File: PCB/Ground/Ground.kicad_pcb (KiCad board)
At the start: 2 copper layers, 100 x 86.6 mm, 39 parts, among them CN1 GROVE, CN2 GROVE, CN3 GROVE, CN4 GROVE, CN5 GROVE, CN6 TTL-232R-3V3, CN7 ST-LINK, CN8 Conn_01x05_Female, CN9 CardEdgeConnector5P, SW1 RESET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

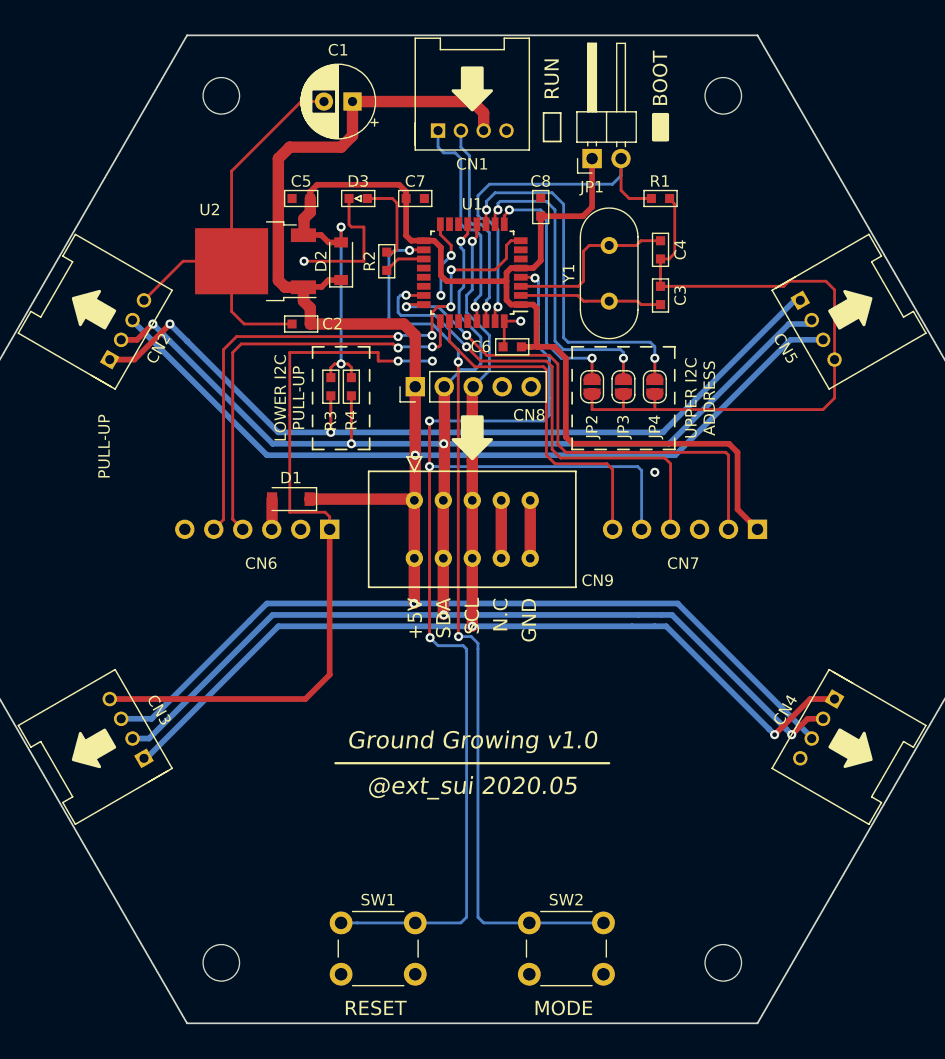
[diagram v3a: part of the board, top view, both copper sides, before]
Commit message: [update] Groundの配線改善(GNDビア) #4
* GNDビアを10mm間隔で配置できる箇所に配置
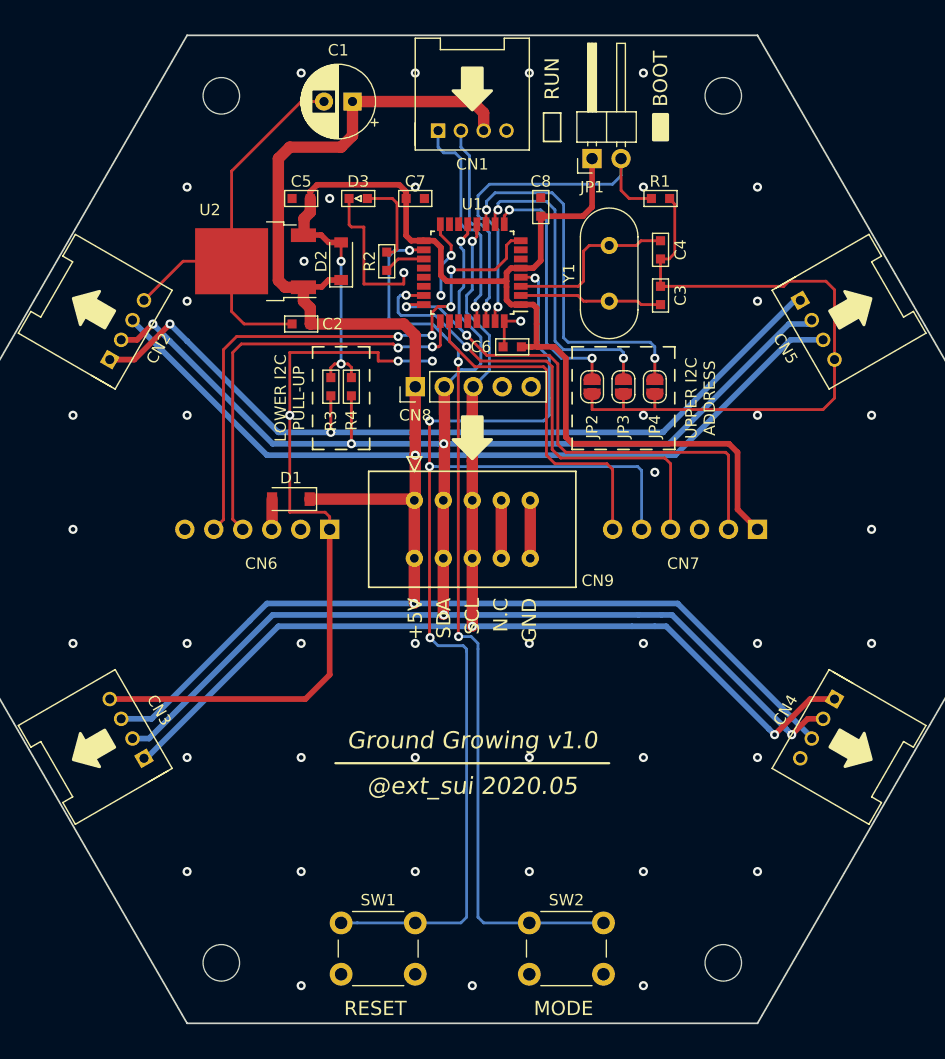
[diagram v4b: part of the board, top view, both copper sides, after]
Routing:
- net 3V3: track 109.0 -> 106.3 mm
- net GND: track 191.7 -> 192.9 mm, vias 7 -> 50
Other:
- board text removed: "PULL-UP"
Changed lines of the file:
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@@
   (general
     (thickness 1.6)
-    (drawings 114)
-    (tracks 506)
+    (drawings 113)
+    (tracks 550)
     (zones 0)
     (modules 39)
@@
   )
   (setup
-    (last_trace_width 0.5)
+    (last_trace_width 0.25)
     (user_trace_width 0.5)
     (user_trace_width 1)
@@
     (descr "Through hole straight pin header, 1x05, 2.54mm pitch, single row")
     (tags "Through hole pin header THT 1x05 2.54mm single row")
-    (fp_text reference CN8 (at -2.5 10 180) (layer F.SilkS)
+    (fp_text reference CN8 (at -2.5 0 180) (layer F.SilkS)
       (effects (font (size 1 1) (thickness 0.15)))
     )
@@
   (gr_line (start 120 89) (end 121 89) (layer F.SilkS) (width 0.15))
   (gr_line (start 121 90) (end 121 89) (layer F.SilkS) (width 0.15))
-  (gr_text PULL-UP (at 97.75 97.75 90) (layer F.SilkS)
-    (effects (font (size 1 1) (thickness 0.15)))
-  )
   (gr_text × (at 132.6 94.8) (layer B.SilkS)
     (effects (font (size 1.75 1.75) (thickness 0.2)) (justify mirror))
@@
   (gr_line (start 105 148.30127) (end 80 105) (layer Edge.Cuts) (width 0.15))
   (gr_line (start 80 105) (end 105 61.69873) (layer Edge.Cuts) (width 0.15))
+  (via (at 124 82.5) (size 0.8) (drill 0.4) (layers F.Cu B.Cu) (net 1))
+  (via (at 117.5 76) (size 0.8) (drill 0.4) (layers F.Cu B.Cu) (net 1))
+  (via (at 155 135) (size 0.8) (drill 0.4) (layers F.Cu B.Cu) (net 1))
   (segment (start 135.08 102.46) (end 135.08 107.54) (width 1) (layer F.Cu) (net 1))
   (segment (start 135.16 102.38) (end 135.08 102.46) (width 0.25) (layer F.Cu) (net 1))
@@
   (segment (start 117.5 105) (end 117.5 103.9) (width 0.25) (layer F.Cu) (net 1))
   (segment (start 117.5 103.9) (end 117.1 103.5) (width 0.25) (layer F.Cu) (net 1))
-  (segment (start 119.2 78.3) (end 119.2 76) (width 0.25) (layer F.Cu) (net 1))
-  (segment (start 119.4 78.5) (end 119.2 78.3) (width 0.25) (layer F.Cu) (net 1))
-  (segment (start 120.5 78.5) (end 119.4 78.5) (width 0.25) (layer F.Cu) (net 1))
-  (segment (start 115.25 81.5) (end 120.5 81.5) (width 0.25) (layer F.Cu) (net 1))
-  (segment (start 120.5 81.5) (end 120.5 78.5) (width 0.25) (layer F.Cu) (net 1))
   (segment (start 114 95) (end 114 89.5) (width 0.25) (layer F.Cu) (net 1))
   (segment (start 114 89.5) (end 121.75 89.5) (width 0.25) (layer F.Cu) (net 1))
@@
   (via (at 126.5 90.25) (size 0.8) (drill 0.4) (layers F.Cu B.Cu) (net 1))
   (segment (start 123.5 90.25) (end 126.5 90.25) (width 0.25) (layer B.Cu) (net 1))
+  (via (at 145 135) (size 0.8) (drill 0.4) (layers F.Cu B.Cu) (net 1))
+  (via (at 135 135) (size 0.8) (drill 0.4) (layers F.Cu B.Cu) (net 1))
+  (via (at 125 135) (size 0.8) (drill 0.4) (layers F.Cu B.Cu) (net 1))
+  (via (at 115 135) (size 0.8) (drill 0.4) (layers F.Cu B.Cu) (net 1))
+  (via (at 105 135) (size 0.8) (drill 0.4) (layers F.Cu B.Cu) (net 1))
+  (via (at 105 125) (size 0.8) (drill 0.4) (layers F.Cu B.Cu) (net 1))
+  (via (at 115 125) (size 0.8) (drill 0.4) (layers F.Cu B.Cu) (net 1))
+  (via (at 125 125) (size 0.8) (drill 0.4) (layers F.Cu B.Cu) (net 1))
+  (via (at 135 125) (size 0.8) (drill 0.4) (layers F.Cu B.Cu) (net 1))
+  (via (at 145 125) (size 0.8) (drill 0.4) (layers F.Cu B.Cu) (net 1))
+  (via (at 155 125) (size 0.8) (drill 0.4) (layers F.Cu B.Cu) (net 1))
+  (via (at 155 115) (size 0.8) (drill 0.4) (layers F.Cu B.Cu) (net 1))
+  (via (at 145 115) (size 0.8) (drill 0.4) (layers F.Cu B.Cu) (net 1))
+  (via (at 135 115) (size 0.8) (drill 0.4) (layers F.Cu B.Cu) (net 1))
+  (via (at 125 115) (size 0.8) (drill 0.4) (layers F.Cu B.Cu) (net 1))
+  (via (at 115 115) (size 0.8) (drill 0.4) (layers F.Cu B.Cu) (net 1))
+  (via (at 105 115) (size 0.8) (drill 0.4) (layers F.Cu B.Cu) (net 1))
+  (via (at 95 115) (size 0.8) (drill 0.4) (layers F.Cu B.Cu) (net 1))
+  (via (at 95 105) (size 0.8) (drill 0.4) (layers F.Cu B.Cu) (net 1))
+  (via (at 95 95) (size 0.8) (drill 0.4) (layers F.Cu B.Cu) (net 1))
+  (via (at 165 115) (size 0.8) (drill 0.4) (layers F.Cu B.Cu) (net 1))
+  (via (at 165 105) (size 0.8) (drill 0.4) (layers F.Cu B.Cu) (net 1))
+  (via (at 165 95) (size 0.8) (drill 0.4) (layers F.Cu B.Cu) (net 1))
+  (via (at 155 95) (size 0.8) (drill 0.4) (layers F.Cu B.Cu) (net 1))
+  (via (at 155 85) (size 0.8) (drill 0.4) (layers F.Cu B.Cu) (net 1))
+  (via (at 155 75) (size 0.8) (drill 0.4) (layers F.Cu B.Cu) (net 1))
+  (via (at 105 95) (size 0.8) (drill 0.4) (layers F.Cu B.Cu) (net 1))
+  (via (at 105 85) (size 0.8) (drill 0.4) (layers F.Cu B.Cu) (net 1))
+  (via (at 105 75) (size 0.8) (drill 0.4) (layers F.Cu B.Cu) (net 1))
+  (via (at 145 145) (size 0.8) (drill 0.4) (layers F.Cu B.Cu) (net 1))
+  (via (at 130 145) (size 0.8) (drill 0.4) (layers F.Cu B.Cu) (net 1))
+  (via (at 115 145) (size 0.8) (drill 0.4) (layers F.Cu B.Cu) (net 1))
+  (via (at 125 65) (size 0.8) (drill 0.4) (layers F.Cu B.Cu) (net 1))
+  (via (at 135 65) (size 0.8) (drill 0.4) (layers F.Cu B.Cu) (net 1))
+  (via (at 115 65) (size 0.8) (drill 0.4) (layers F.Cu B.Cu) (net 1))
+  (via (at 145 75) (size 0.8) (drill 0.4) (layers F.Cu B.Cu) (net 1))
+  (via (at 145 65) (size 0.8) (drill 0.4) (layers F.Cu B.Cu) (net 1))
+  (via (at 125 75) (size 0.8) (drill 0.4) (layers F.Cu B.Cu) (net 1))
+  (via (at 145 95) (size 0.8) (drill 0.4) (layers F.Cu B.Cu) (net 1))
+  (via (at 114 95) (size 0.8) (drill 0.4) (layers F.Cu B.Cu) (net 1))
+  (segment (start 119.2 78.3) (end 119.2 76) (width 0.25) (layer F.Cu) (net 1))
+  (segment (start 119.4 78.5) (end 119.2 78.3) (width 0.25) (layer F.Cu) (net 1))
+  (segment (start 120.5 78.5) (end 119.4 78.5) (width 0.25) (layer F.Cu) (net 1))
+  (segment (start 120.5 83.5) (end 120.5 78.5) (width 0.25) (layer F.Cu) (net 1))
+  (segment (start 124 82.5) (end 124 83.5) (width 0.25) (layer F.Cu) (net 1))
+  (segment (start 124 83.5) (end 120.5 83.5) (width 0.25) (layer F.Cu) (net 1))
   (segment (start 124.92 102.46) (end 124.92 107.54) (width 1) (layer F.Cu) (net 4))
   (segment (start 125 92.5) (end 125 96.5) (width 1) (layer F.Cu) (net 4))
@@
   (segment (start 138.2 90) (end 138.2 96.9) (width 0.5) (layer F.Cu) (net 7))
   (segment (start 138.2 96.9) (end 138.8 97.5) (width 0.5) (layer F.Cu) (net 7))
-  (via (at 118.5 78.5) (size 0.8) (drill 0.4) (layers F.Cu B.Cu) (net 7))
-  (segment (start 118.5 79.85) (end 118.5 78.5) (width 0.25) (layer F.Cu) (net 7))
   (via (at 118.5 90.5) (size 0.8) (drill 0.4) (layers F.Cu B.Cu) (net 7))
-  (segment (start 118.5 78.5) (end 118.5 90.5) (width 0.25) (layer B.Cu) (net 7))
   (segment (start 118.5 90.5) (end 119.1 90.5) (width 0.25) (layer F.Cu) (net 7))
   (segment (start 119.4 90.8) (end 119.4 91.7) (width 0.25) (layer F.Cu) (net 7))
@@
   (segment (start 153.25 98.25) (end 153.25 103.25) (width 0.5) (layer F.Cu) (net 7))
   (segment (start 153.25 103.25) (end 155 105) (width 0.5) (layer F.Cu) (net 7))
+  (segment (start 118.5 81.5) (end 118.5 90.5) (width 0.25) (layer B.Cu) (net 7))
+  (via (at 118.5 81.5) (size 0.8) (drill 0.4) (layers F.Cu B.Cu) (net 7))
+  (segment (start 118.5 79.85) (end 118.5 81.5) (width 0.25) (layer F.Cu) (net 7))
   (via (at 130.25 85.5) (size 0.8) (drill 0.4) (layers F.Cu B.Cu) (net 8))
   (segment (start 130.4 86.75) (end 130.4 85.65) (width 0.25) (layer F.Cu) (net 8))
